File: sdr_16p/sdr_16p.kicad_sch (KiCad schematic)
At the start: 11 parts, among them J1 Rx, J10 ADAU1467_GPIOS, J11 ADAU1467_AUX_ADCS, J2 Tx, J4 6V, J6 Microcontroller, J7 USBi, J8 I2S2, J9 I2S1

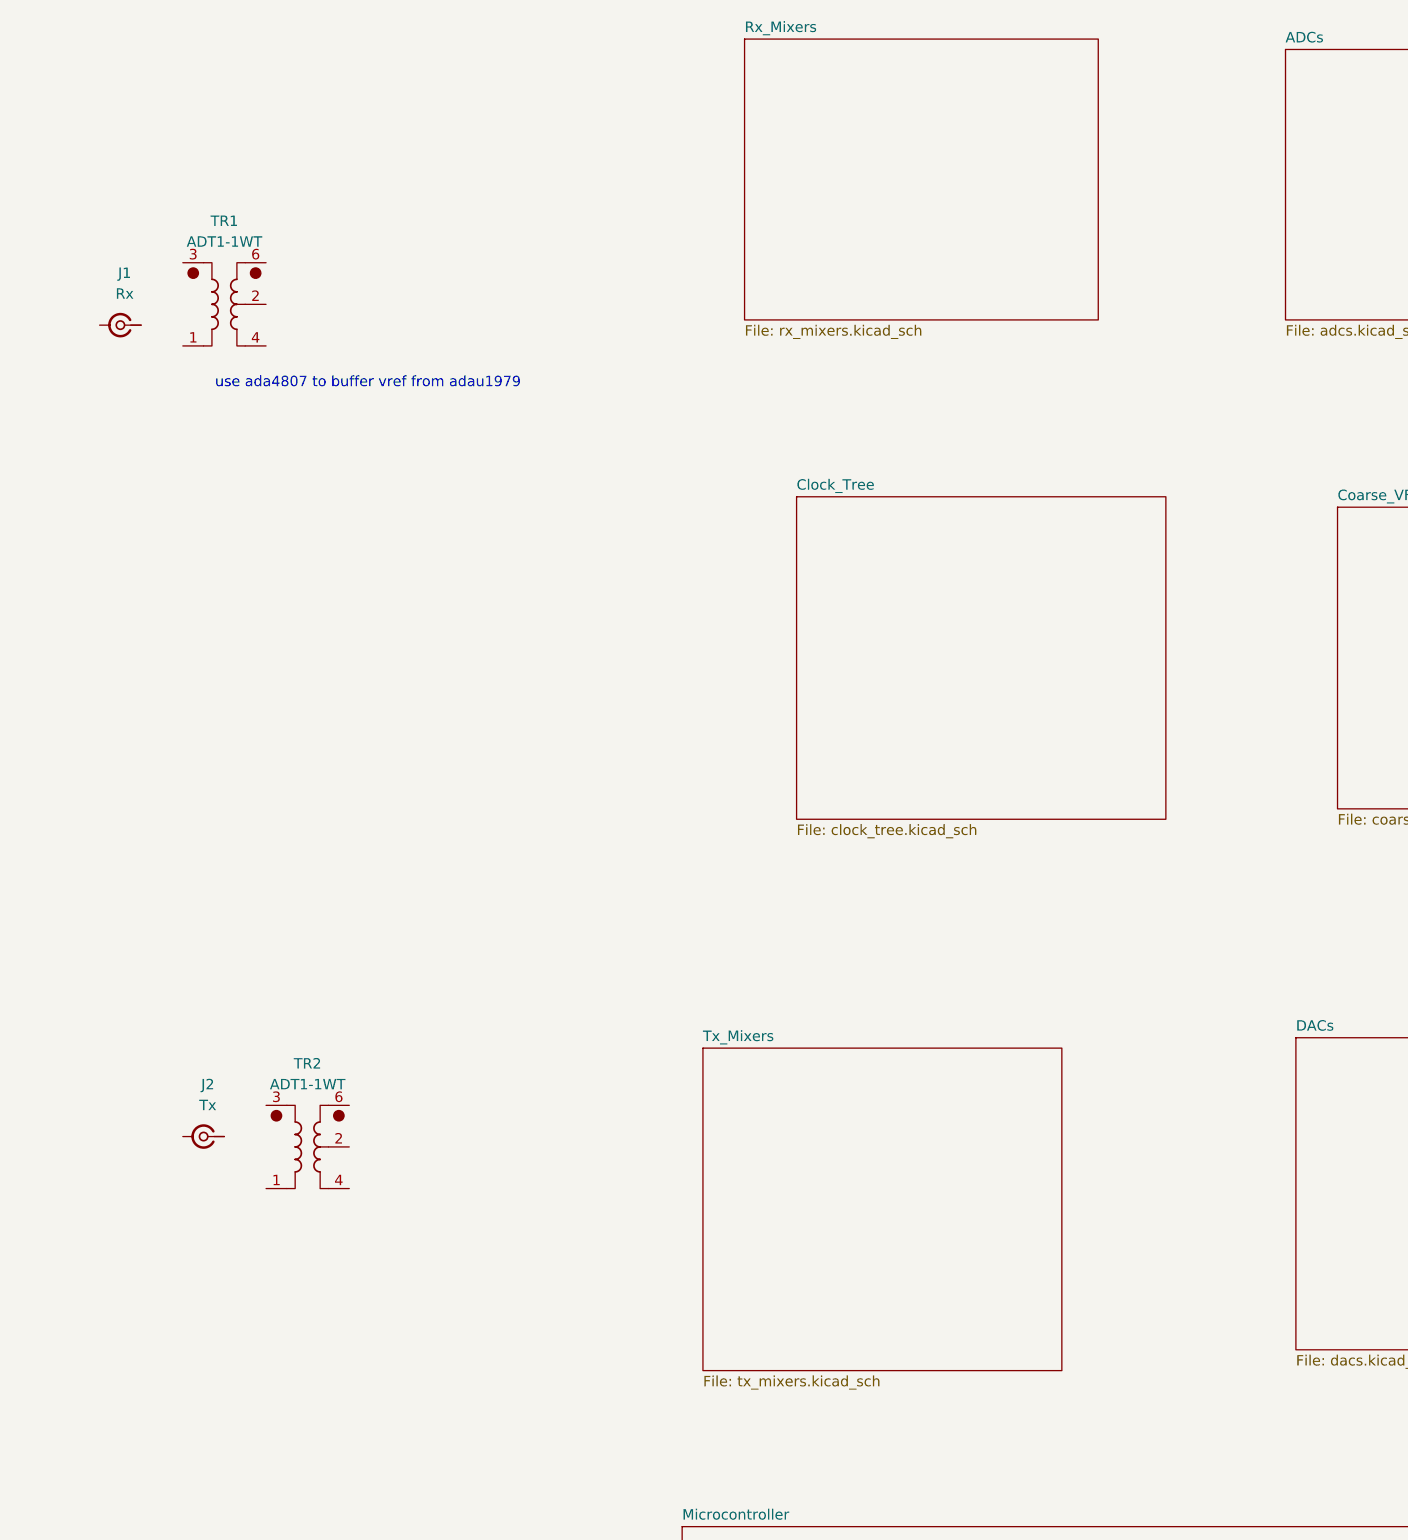
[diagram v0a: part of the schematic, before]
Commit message: updated to 16 channel SE
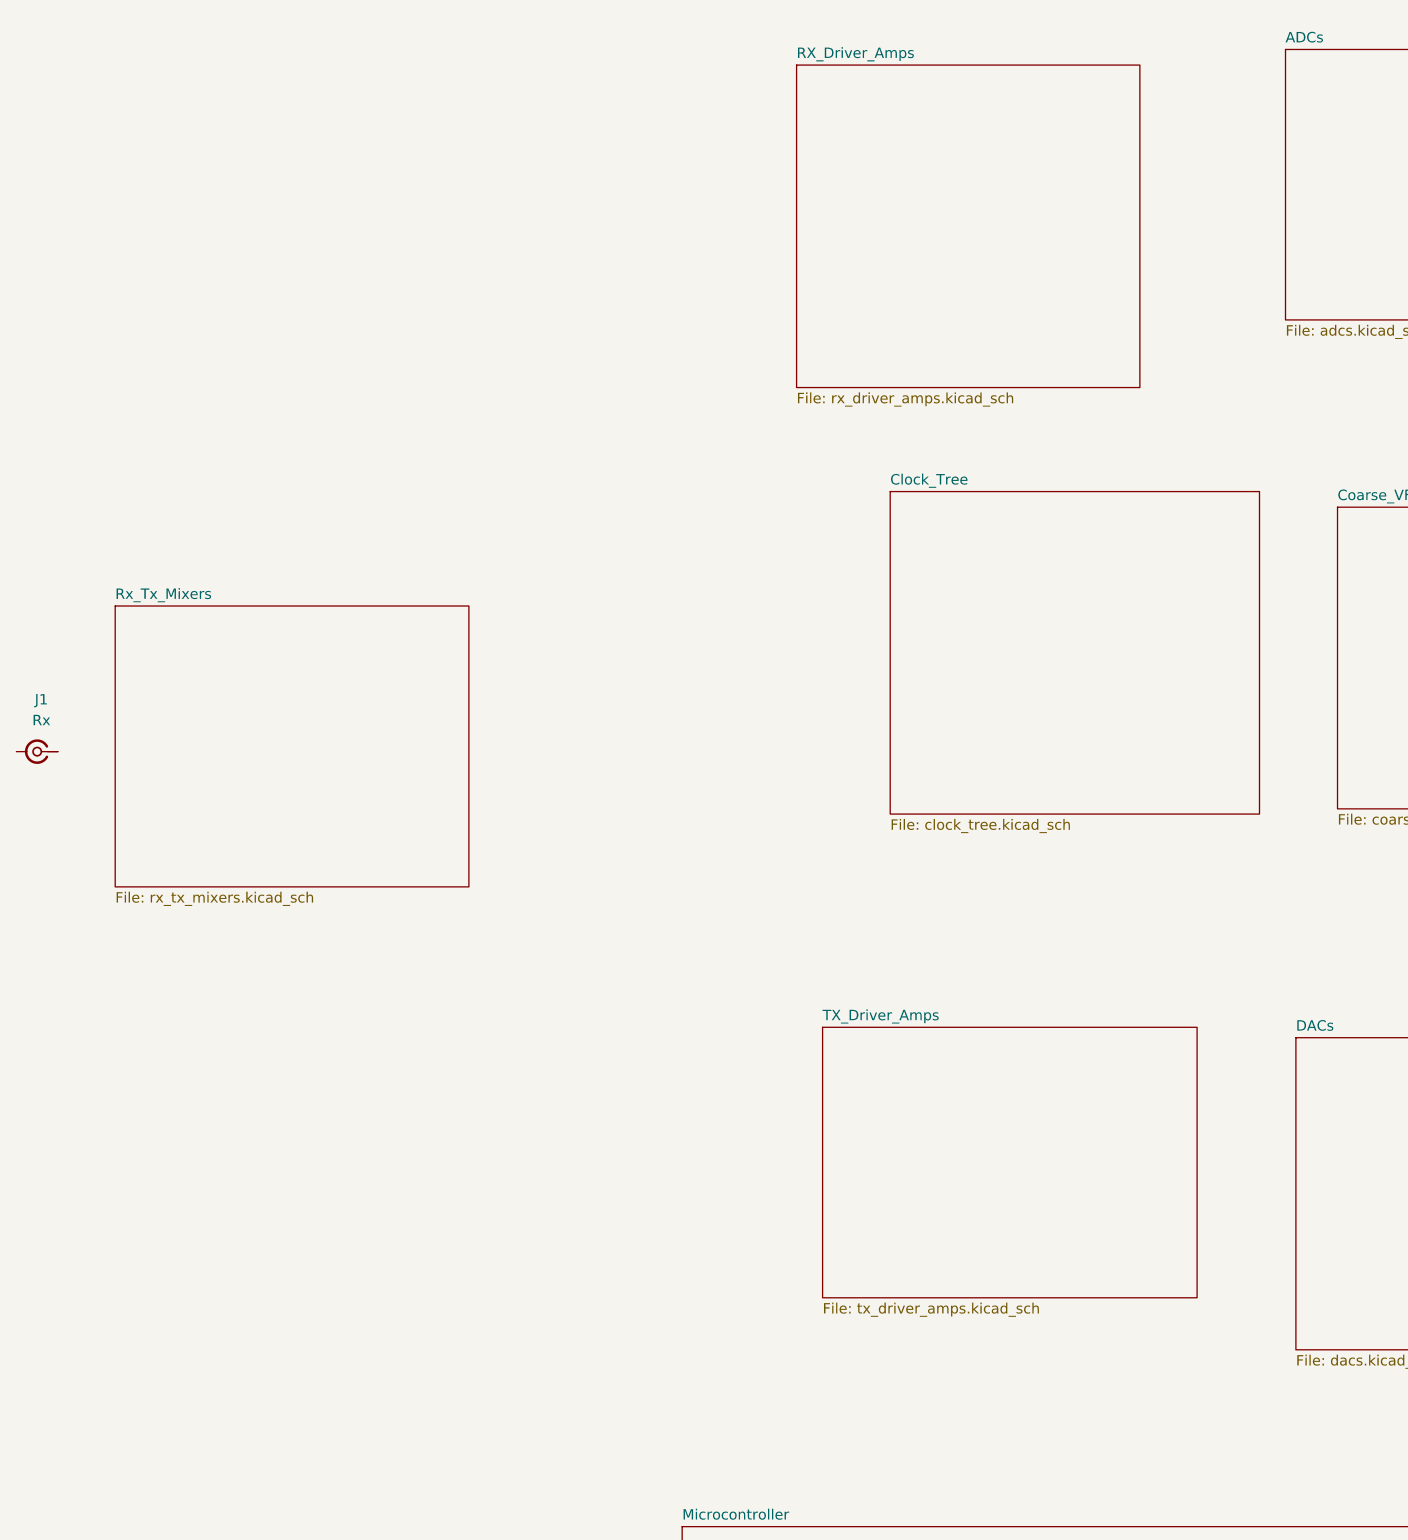
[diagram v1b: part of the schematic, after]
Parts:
- removed J2: Tx, symbol Connector:Conn_Coaxial_Small
- removed TR1, TR2: ADT1-1WT, RF_Mini-Circuits:Mini-Circuits_CD542_H2.84mm, symbol Transformer:ADT1-1WT
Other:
- sheet Rx_Mixers renamed Rx_Tx_Mixers
- removed sheet Tx_Mixers
- added sheet RX_Driver_Amps (rx_driver_amps.kicad_sch)
- added sheet TX_Driver_Amps (tx_driver_amps.kicad_sch)
- sheet Rx_Tx_Mixers: file rx_mixers.kicad_sch -> rx_tx_mixers.kicad_sch
- note removed: "use ada4807 to buffer vref from adau1979"
- moved on the sheet: J1
